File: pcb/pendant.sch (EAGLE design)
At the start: 10 parts, among them IC1 TINY22S

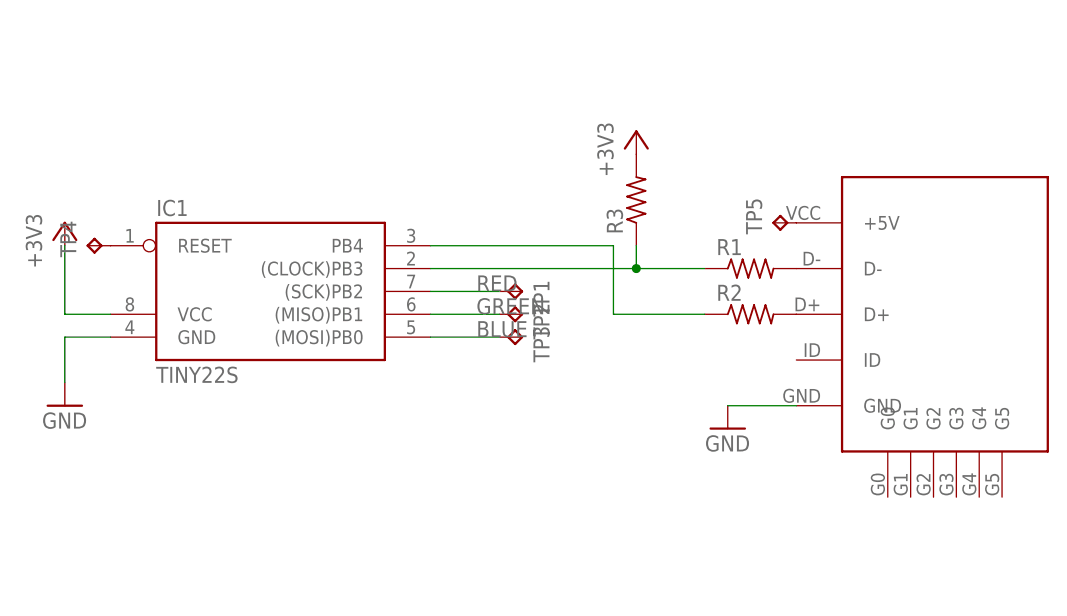
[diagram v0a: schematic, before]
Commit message: added square cutout magnet, worked on board outline
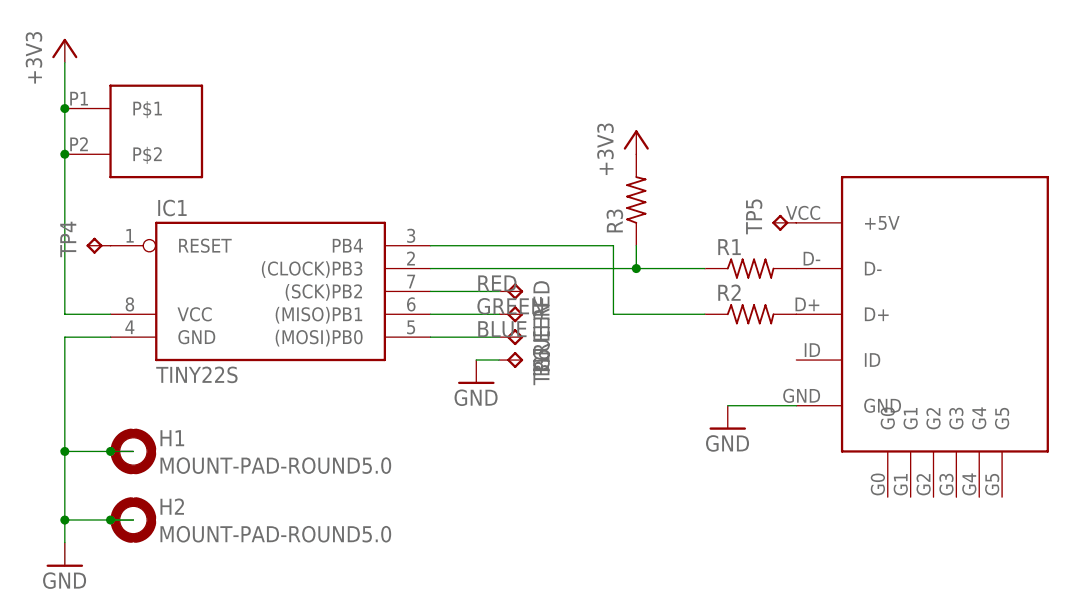
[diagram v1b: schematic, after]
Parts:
- added H1, H2: MOUNT-PAD-ROUND5.0, holes:MOUNT-PAD-ROUND5.0
- added TP6: TPPAD1-13, testpad:TPPAD1-13
- added U$2: MAGNET, pendant:MAGNET
- renumbered TP1 to RED, TP2 to GREEN, TP3 to BLUE
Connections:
- net +3V3: now also U$2.P$1, U$2.P$2
- net GND: now also H1.MOUNT, H2.MOUNT, TP6.TP
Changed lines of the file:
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@@
 <part name="+3V1" library="supply1" deviceset="+3V3" device=""/>
 <part name="+3V2" library="supply1" deviceset="+3V3" device=""/>
-<part name="TP1" library="testpad" deviceset="TP" device="PAD1-13"/>
-<part name="TP2" library="testpad" deviceset="TP" device="PAD1-13"/>
-<part name="TP3" library="testpad" deviceset="TP" device="PAD1-13"/>
+<part name="RED" library="testpad" deviceset="TP" device="PAD1-13"/>
+<part name="GREEN" library="testpad" deviceset="TP" device="PAD1-13"/>
+<part name="BLUE" library="testpad" deviceset="TP" device="PAD1-13"/>
 <part name="TP4" library="testpad" deviceset="TP" device="PAD1-13"/>
 <part name="TP5" library="testpad" deviceset="TP" device="PAD1-13"/>
+<part name="H1" library="holes" deviceset="MOUNT-PAD-ROUND" device="5.0"/>
+<part name="H2" library="holes" deviceset="MOUNT-PAD-ROUND" device="5.0"/>
+<part name="TP6" library="testpad" deviceset="TP" device="PAD1-13"/>
+<part name="GND2" library="supply1" deviceset="GND" device=""/>
+<part name="U$2" library="pendant" deviceset="MAGNET" device=""/>
 </parts>
 <sheets>
@@
 <instance part="R2" gate="G$1" x="127" y="58.42"/>
 <instance part="R3" gate="G$1" x="114.3" y="71.12" rot="R90"/>
-<instance part="GND1" gate="1" x="50.8" y="48.26"/>
+<instance part="GND1" gate="1" x="50.8" y="30.48"/>
 <instance part="GND8" gate="1" x="124.46" y="45.72"/>
-<instance part="+3V1" gate="G$1" x="50.8" y="68.58"/>
+<instance part="+3V1" gate="G$1" x="50.8" y="88.9"/>
 <instance part="+3V2" gate="G$1" x="114.3" y="78.74"/>
-<instance part="TP1" gate="G$1" x="101.6" y="60.96" rot="R270"/>
-<instance part="TP2" gate="G$1" x="101.6" y="58.42" rot="R270"/>
-<instance part="TP3" gate="G$1" x="101.6" y="55.88" rot="R270"/>
+<instance part="RED" gate="G$1" x="101.6" y="60.96" rot="R270"/>
+<instance part="GREEN" gate="G$1" x="101.6" y="58.42" rot="R270"/>
+<instance part="BLUE" gate="G$1" x="101.6" y="55.88" rot="R270"/>
 <instance part="TP4" gate="G$1" x="53.34" y="66.04" rot="R90"/>
 <instance part="TP5" gate="G$1" x="129.54" y="68.58" rot="R90"/>
+<instance part="H1" gate="G$1" x="58.42" y="43.18"/>
+<instance part="H2" gate="G$1" x="58.42" y="35.56"/>
+<instance part="TP6" gate="G$1" x="101.6" y="53.34" rot="R270"/>
+<instance part="GND2" gate="1" x="96.52" y="50.8"/>
+<instance part="U$2" gate="G$1" x="60.96" y="78.74"/>
 </instances>
 <busses>
@@
 <pinref part="GND1" gate="1" pin="GND"/>
 <wire x1="55.88" y1="55.88" x2="50.8" y2="55.88" width="0.1524" layer="91"/>
-<wire x1="50.8" y1="55.88" x2="50.8" y2="50.8" width="0.1524" layer="91"/>
+<wire x1="50.8" y1="55.88" x2="50.8" y2="43.18" width="0.1524" layer="91"/>
+<wire x1="50.8" y1="43.18" x2="50.8" y2="35.56" width="0.1524" layer="91"/>
+<wire x1="50.8" y1="35.56" x2="50.8" y2="33.02" width="0.1524" layer="91"/>
+<wire x1="58.42" y1="35.56" x2="55.88" y2="35.56" width="0.1524" layer="91"/>
+<junction x="50.8" y="35.56"/>
+<wire x1="55.88" y1="35.56" x2="50.8" y2="35.56" width="0.1524" layer="91"/>
+<wire x1="58.42" y1="43.18" x2="55.88" y2="43.18" width="0.1524" layer="91"/>
+<junction x="50.8" y="43.18"/>
+<pinref part="H1" gate="G$1" pin="MOUNT"/>
+<wire x1="55.88" y1="43.18" x2="50.8" y2="43.18" width="0.1524" layer="91"/>
+<junction x="55.88" y="43.18"/>
+<pinref part="H2" gate="G$1" pin="MOUNT"/>
+<junction x="55.88" y="35.56"/>
+</segment>
+<segment>
+<pinref part="TP6" gate="G$1" pin="TP"/>
+<pinref part="GND2" gate="1" pin="GND"/>
+<wire x1="99.06" y1="53.34" x2="96.52" y2="53.34" width="0.1524" layer="91"/>
 </segment>
 </net>
@@
 <pinref part="+3V1" gate="G$1" pin="+3V3"/>
 <wire x1="55.88" y1="58.42" x2="50.8" y2="58.42" width="0.1524" layer="91"/>
-<wire x1="50.8" y1="58.42" x2="50.8" y2="66.04" width="0.1524" layer="91"/>
+<wire x1="50.8" y1="58.42" x2="50.8" y2="76.2" width="0.1524" layer="91"/>
+<pinref part="U$2" gate="G$1" pin="P$1"/>
+<junction x="50.8" y="81.28"/>
+<wire x1="50.8" y1="76.2" x2="50.8" y2="81.28" width="0.1524" layer="91"/>
+<wire x1="50.8" y1="81.28" x2="50.8" y2="86.36" width="0.1524" layer="91"/>
+<pinref part="U$2" gate="G$1" pin="P$2"/>
+<junction x="50.8" y="76.2"/>
 </segment>
 </net>
@@
 <wire x1="91.44" y1="60.96" x2="99.06" y2="60.96" width="0.1524" layer="91"/>
 <label x="96.52" y="60.96" size="1.778" layer="95"/>
-<pinref part="TP1" gate="G$1" pin="TP"/>
+<pinref part="RED" gate="G$1" pin="TP"/>
 </segment>
 </net>
@@
 <wire x1="91.44" y1="58.42" x2="99.06" y2="58.42" width="0.1524" layer="91"/>
 <label x="96.52" y="58.42" size="1.778" layer="95"/>
-<pinref part="TP2" gate="G$1" pin="TP"/>
+<pinref part="GREEN" gate="G$1" pin="TP"/>
 </segment>
 </net>
@@
 <wire x1="91.44" y1="55.88" x2="99.06" y2="55.88" width="0.1524" layer="91"/>
 <label x="96.52" y="55.88" size="1.778" layer="95"/>
-<pinref part="TP3" gate="G$1" pin="TP"/>
+<pinref part="BLUE" gate="G$1" pin="TP"/>
 </segment>
 </net>

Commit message: switch to 8th-inch magnet
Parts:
- U$2: value MAGNET -> MAGNET8TH-INCH; device pendant:MAGNET -> pendant:MAGNET8TH-INCH
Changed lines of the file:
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@@
 <part name="TP6" library="testpad" deviceset="TP" device="PAD1-13"/>
 <part name="GND2" library="supply1" deviceset="GND" device=""/>
-<part name="U$2" library="pendant" deviceset="MAGNET" device=""/>
+<part name="U$2" library="pendant" deviceset="MAGNET" device="8TH-INCH" value="MAGNET8TH-INCH"/>
 </parts>
 <sheets>

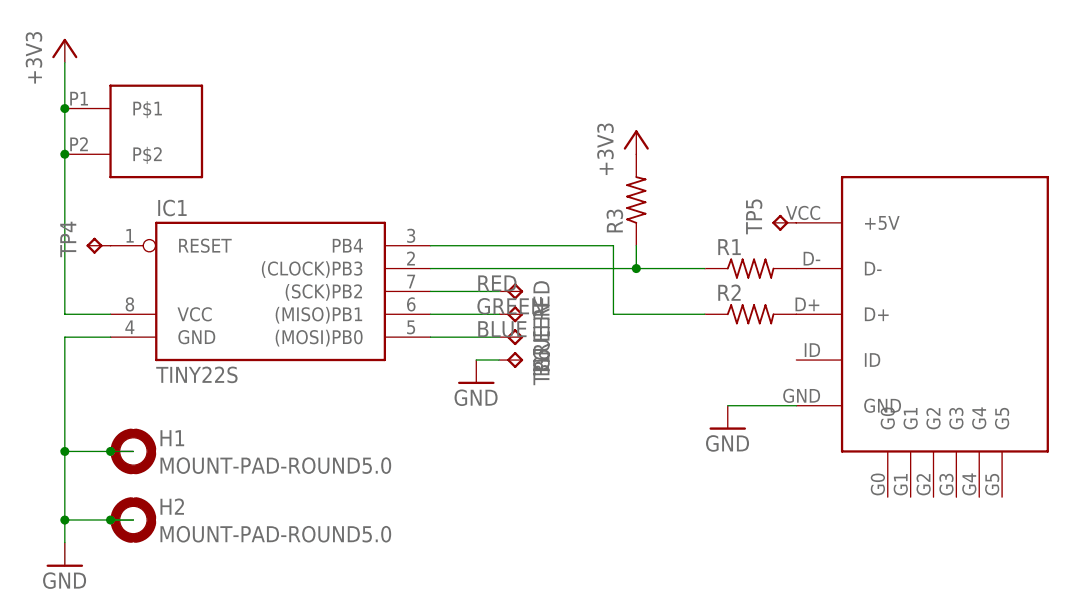
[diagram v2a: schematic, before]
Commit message: fix usb wiring bug; fully routed
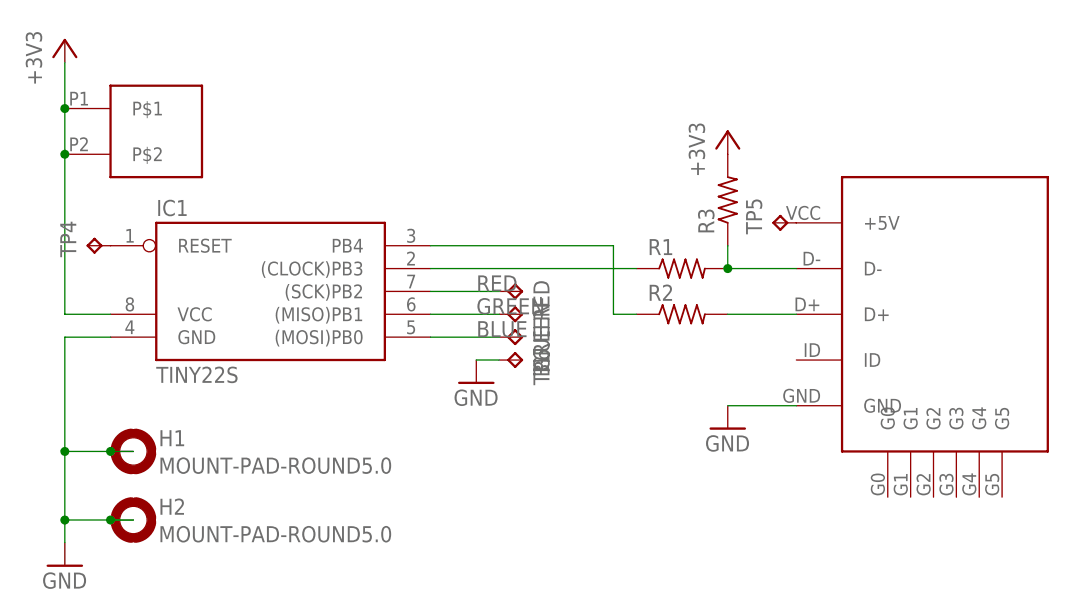
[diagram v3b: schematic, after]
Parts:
- TP5: value TPPAD1-13 -> TPTP10SQ; device testpad:TPPAD1-13 -> testpad:TPTP10SQ
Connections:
- net N$1: now also R3.1
- net N$3: no longer R3.1
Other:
- moved on the sheet: R1, R2, R3
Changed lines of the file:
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@@
 <part name="BLUE" library="testpad" deviceset="TP" device="PAD1-13"/>
 <part name="TP4" library="testpad" deviceset="TP" device="PAD1-13"/>
-<part name="TP5" library="testpad" deviceset="TP" device="PAD1-13"/>
+<part name="TP5" library="testpad" deviceset="TP" device="TP10SQ" value="TPTP10SQ"/>
 <part name="H1" library="holes" deviceset="MOUNT-PAD-ROUND" device="5.0"/>
 <part name="H2" library="holes" deviceset="MOUNT-PAD-ROUND" device="5.0"/>
@@
 <instance part="IC1" gate="G$1" x="73.66" y="60.96"/>
 <instance part="U$1" gate="G$1" x="147.32" y="58.42"/>
-<instance part="R1" gate="G$1" x="127" y="63.5"/>
-<instance part="R2" gate="G$1" x="127" y="58.42"/>
-<instance part="R3" gate="G$1" x="114.3" y="71.12" rot="R90"/>
+<instance part="R1" gate="G$1" x="119.38" y="63.5"/>
+<instance part="R2" gate="G$1" x="119.38" y="58.42"/>
+<instance part="R3" gate="G$1" x="124.46" y="71.12" rot="R90"/>
 <instance part="GND1" gate="1" x="50.8" y="30.48"/>
 <instance part="GND8" gate="1" x="124.46" y="45.72"/>
 <instance part="+3V1" gate="G$1" x="50.8" y="88.9"/>
-<instance part="+3V2" gate="G$1" x="114.3" y="78.74"/>
+<instance part="+3V2" gate="G$1" x="124.46" y="78.74"/>
 <instance part="RED" gate="G$1" x="101.6" y="60.96" rot="R270"/>
 <instance part="GREEN" gate="G$1" x="101.6" y="58.42" rot="R270"/>
@@
 <pinref part="U$1" gate="G$1" pin="D-"/>
 <pinref part="R1" gate="G$1" pin="2"/>
+<wire x1="124.46" y1="63.5" x2="132.08" y2="63.5" width="0.1524" layer="91"/>
+<pinref part="R3" gate="G$1" pin="1"/>
+<wire x1="124.46" y1="66.04" x2="124.46" y2="63.5" width="0.1524" layer="91"/>
+<junction x="124.46" y="63.5"/>
 </segment>
 </net>
@@
 <pinref part="U$1" gate="G$1" pin="D+"/>
 <pinref part="R2" gate="G$1" pin="2"/>
+<wire x1="124.46" y1="58.42" x2="132.08" y2="58.42" width="0.1524" layer="91"/>
 </segment>
 </net>
@@
 <segment>
 <pinref part="R1" gate="G$1" pin="1"/>
-<pinref part="R3" gate="G$1" pin="1"/>
-<wire x1="121.92" y1="63.5" x2="114.3" y2="63.5" width="0.1524" layer="91"/>
-<wire x1="114.3" y1="63.5" x2="114.3" y2="66.04" width="0.1524" layer="91"/>
 <pinref part="IC1" gate="G$1" pin="(CLOCK)PB3"/>
 <wire x1="91.44" y1="63.5" x2="114.3" y2="63.5" width="0.1524" layer="91"/>
-<junction x="114.3" y="63.5"/>
 </segment>
 </net>
@@
 <wire x1="111.76" y1="66.04" x2="111.76" y2="58.42" width="0.1524" layer="91"/>
 <pinref part="R2" gate="G$1" pin="1"/>
-<wire x1="111.76" y1="58.42" x2="121.92" y2="58.42" width="0.1524" layer="91"/>
+<wire x1="111.76" y1="58.42" x2="114.3" y2="58.42" width="0.1524" layer="91"/>
 </segment>
 </net>
